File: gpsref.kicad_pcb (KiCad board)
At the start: 4 copper layers, 79.8 x 47.2 mm, 150 parts, among them J13 Boot, J2 SMA, J3 SMA, J4 SMA, J5 U.Fl, J6 SMA, J7 USB_C_Receptacle_16P, J8 U.Fl, J9 U.Fl, Q1 AO3400A, Q2 AO3401A, T2 MABA-010247-2R1250, U1 MAX-M10S, U11 74LVC1G07, U2 LMK05318BRGZR, U21 TMP117xxDRV, U3 TG5032CGN, U31 TLV3601DCKR, U32 TLV3601DCKR, U4 STM32H503KBUx, U5 TPS82084SIL, U6 TPS82084SIL, U7 TPS7A8801RTJR

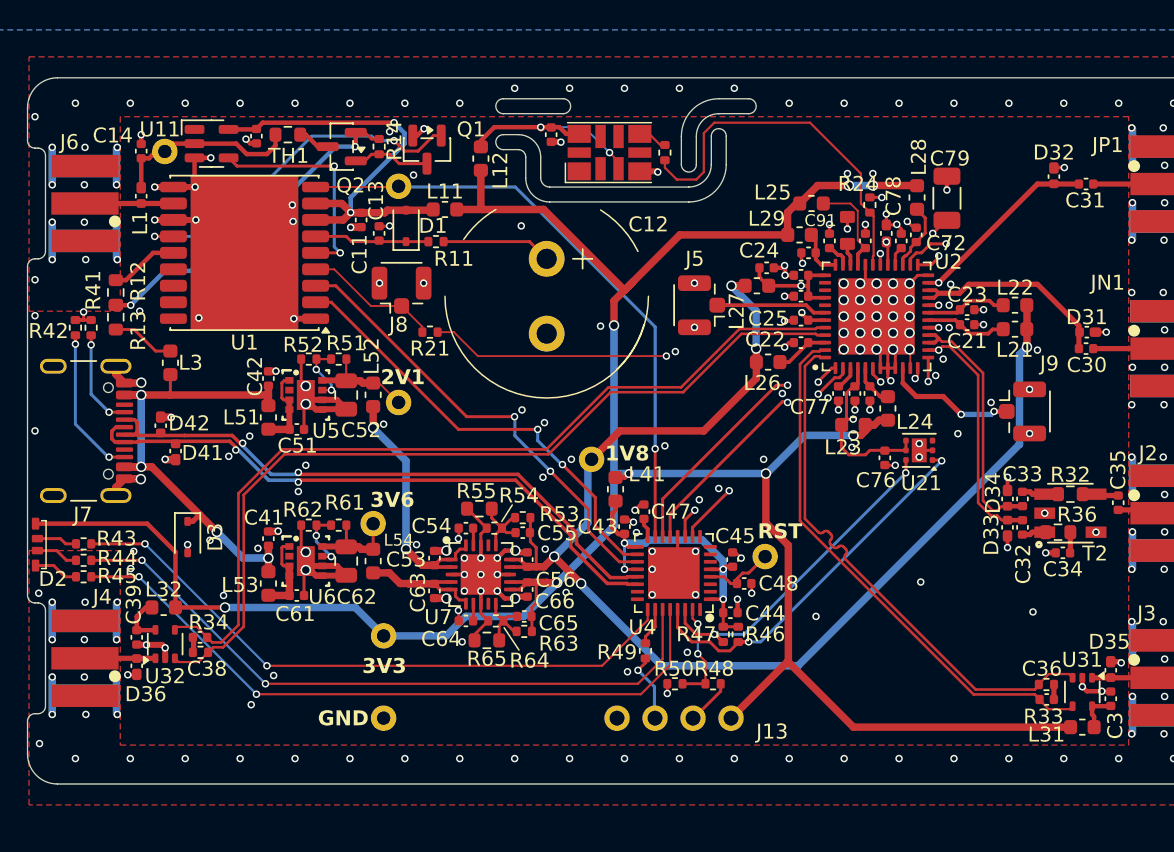
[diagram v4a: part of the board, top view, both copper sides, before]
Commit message: Skedd connector is back.
Route I2C to GPS and hook in the alert line.
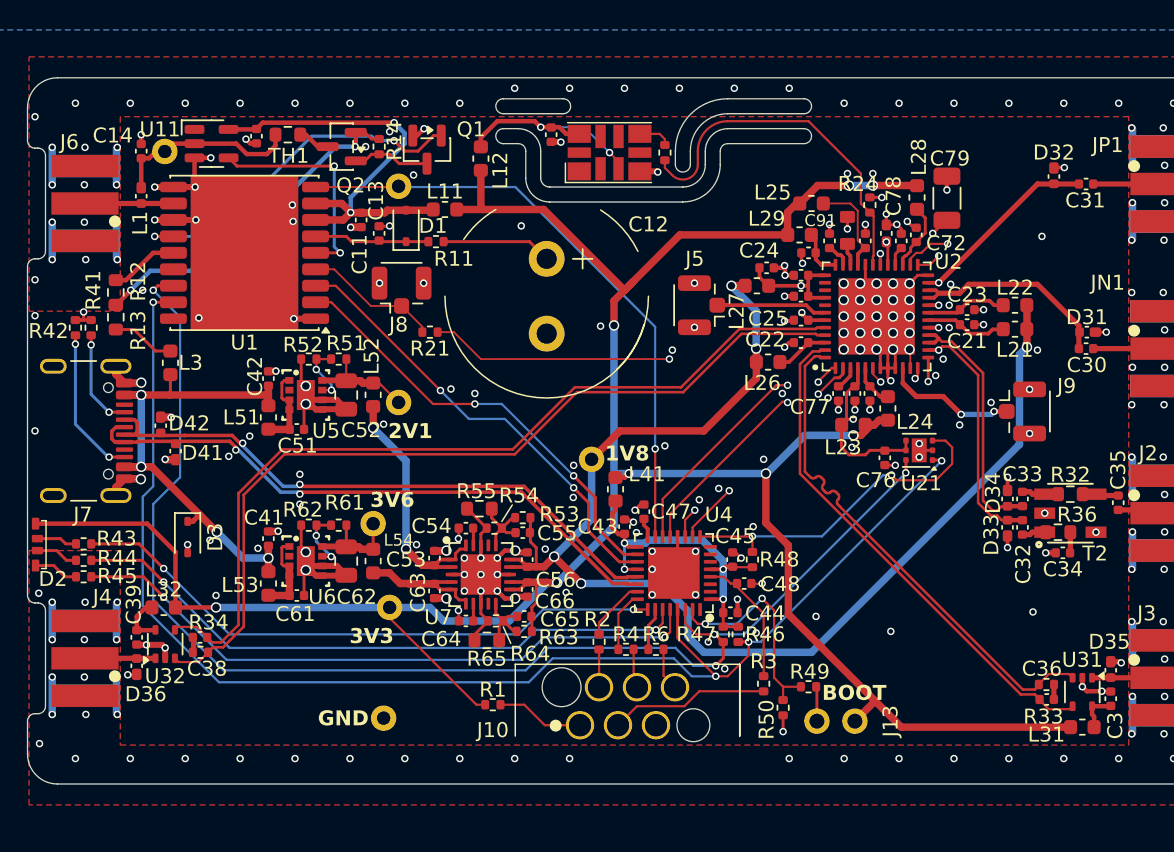
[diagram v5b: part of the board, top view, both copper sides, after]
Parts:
- removed the R49 at (140.1, 114.7)
- removed TP8: TestPoint_Probe, Parts:TestPoint
- added J10: Skedd, Parts:Skedd6, F.Cu at (138.9, 118.4)
- added R1: 100, Resistor_SMD:R_0402_1005Metric, F.Cu at (129.9, 118.3)
- added R2: 100, Resistor_SMD:R_0402_1005Metric, F.Cu at (137.0, 114.1)
- added R3: 100, Resistor_SMD:R_0402_1005Metric, F.Cu at (148.0, 116.9)
- added R4: 100, Resistor_SMD:R_0402_1005Metric, F.Cu at (138.8, 114.6)
- added R48: 10k, Resistor_SMD:R_0402_1005Metric, F.Cu at (147.2, 108.6)
- added R6: 100, Resistor_SMD:R_0402_1005Metric, F.Cu at (140.8, 114.6)
- J13: footprint Parts:PinHeader_1x04_P2.54mm_Vertical -> Parts:PinHeader_1x02_P2.54mm_Vertical
- moved J13 8.28 mm to (154.1, 119.4)
- moved R50 7.40 mm to (149.3, 118.5), turned to -90 degrees
- moved R49 6.38 mm to (151.0, 117.1)
- moved TP7 1.94 mm to (123.0, 111.8)
- renumbered R48 to R49
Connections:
- U1 pad 16: unconnected-(U1-SDA-Pad16) -> I2C_SDA
- U1 pad 17: unconnected-(U1-SCL-Pad17) -> I2C_SCL
- U21 pad 3: unconnected-(U21-ALERT-Pad3) -> ALERT
- U4 pad 23: unconnected-(U4-PA13(JTMS-Pad23) -> /CPU/SWDIO
- U4 pad 24: unconnected-(U4-PA14(JTCK-Pad24) -> /CPU/SWCLK
- U4 pad 9: unconnected-(U4-PA3-Pad9) -> ALERT
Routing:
- net I2C_SDA: track 43.1 -> 108.4 mm, vias 3 -> 5
- net I2C_SCL: track 47.4 -> 112.3 mm, vias 3 -> 5
- net ALERT: track 0.00 -> 22.8 mm, vias 0 -> 2
- net /CPU/dRST: track 0.00 -> 10.7 mm
- net /CPU/BOOT0: track 6.85 -> 14.7 mm
- net /Clocking/XO_P: track 24.9 -> 18.9 mm
- net /CPU/d3V3: track 0.00 -> 5.88 mm
- net /CPU/SWDIO: track 0.00 -> 4.20 mm
- net /CPU/CPU_nRST: track 4.78 -> 8.90 mm
- net /CPU/SWCLK: track 0.00 -> 4.06 mm
- net /CPU/Green: track 45.6 -> 42.2 mm
- net +3V3: track 171.4 -> 174.7 mm
- net /CPU/Red: track 46.5 -> 43.3 mm
- net /CPU/dSWC: track 0.00 -> 2.62 mm
- net /CPU/dSWD: track 0.00 -> 2.52 mm
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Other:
- outline, holes or cut-outs redrawn
- board text added: "BOOT"
- board text removed: "RST"

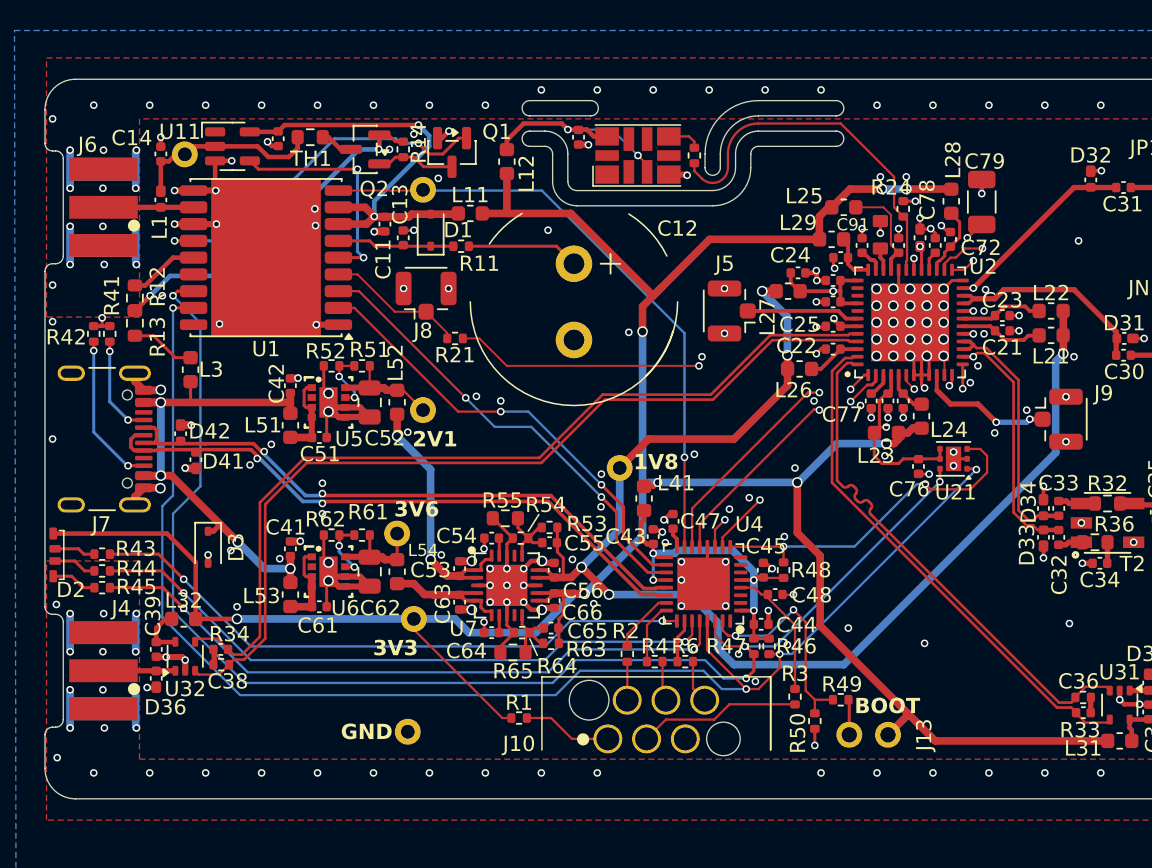
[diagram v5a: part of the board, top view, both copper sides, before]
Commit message: Route extint.
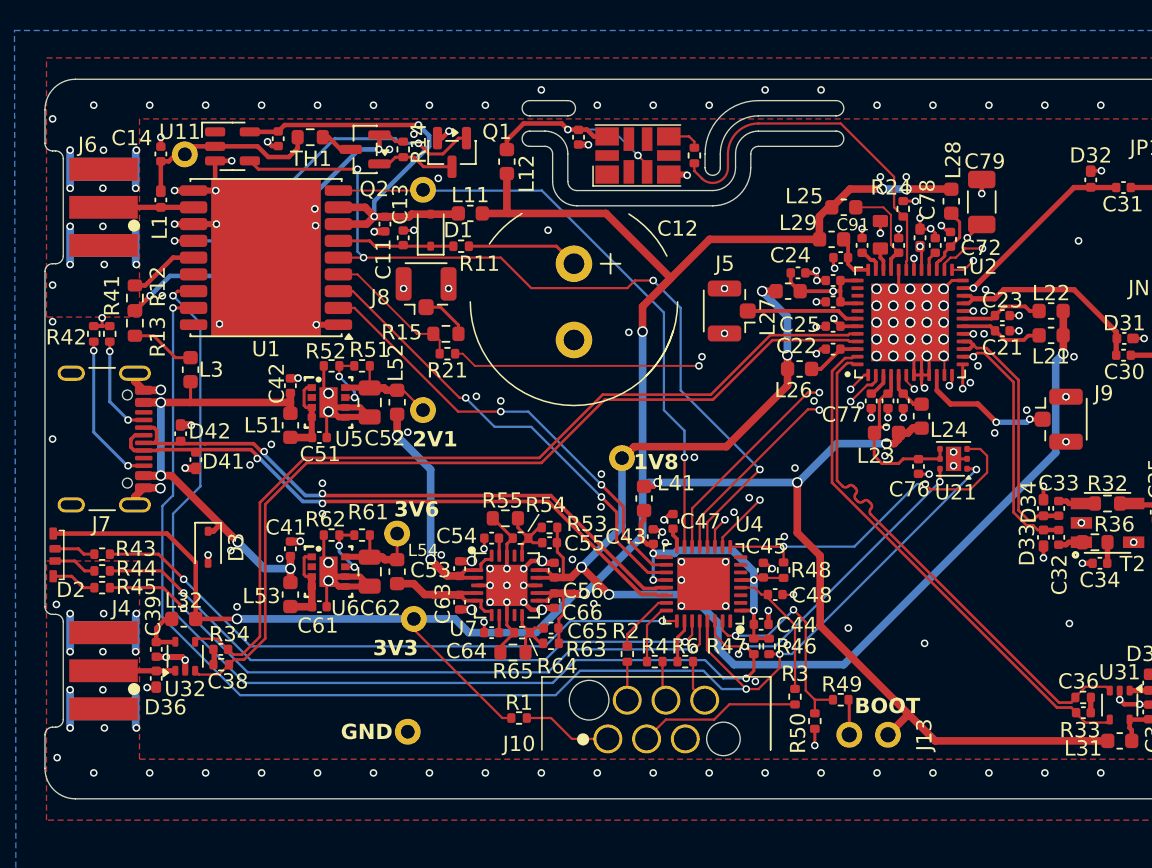
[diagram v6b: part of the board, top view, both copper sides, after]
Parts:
- added R15: 0, Resistor_SMD:R_0603_1608Metric, F.Cu at (125.1, 93.1)
- moved R21 1.12 mm to (125.2, 94.4)
- moved TP6 0.67 mm to (136.7, 101.2)
- moved J8 0.30 mm to (123.8, 90.3)
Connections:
- J8 pad 1: GPSCLK -> Net-(J8-In)
- U1 pad 5: /GPS/EXTINT -> EXTINT
- U11 pad 4: /GPS/EXTINT -> EXTINT
- U4 pad 12: GND -> EXTINT
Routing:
- net EXTINT: track 0.00 -> 56.7 mm, vias 0 -> 4
- net /GPS/EXTINT: track 14.9 -> 0.00 mm, vias 2 -> 0
- net Net-(J8-In): track 0.00 -> 3.19 mm
- net GND: track 168.7 -> 166.4 mm, vias 286 -> 289
- net OUT5: track 7.41 -> 8.04 mm
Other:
- outline, holes or cut-outs redrawn

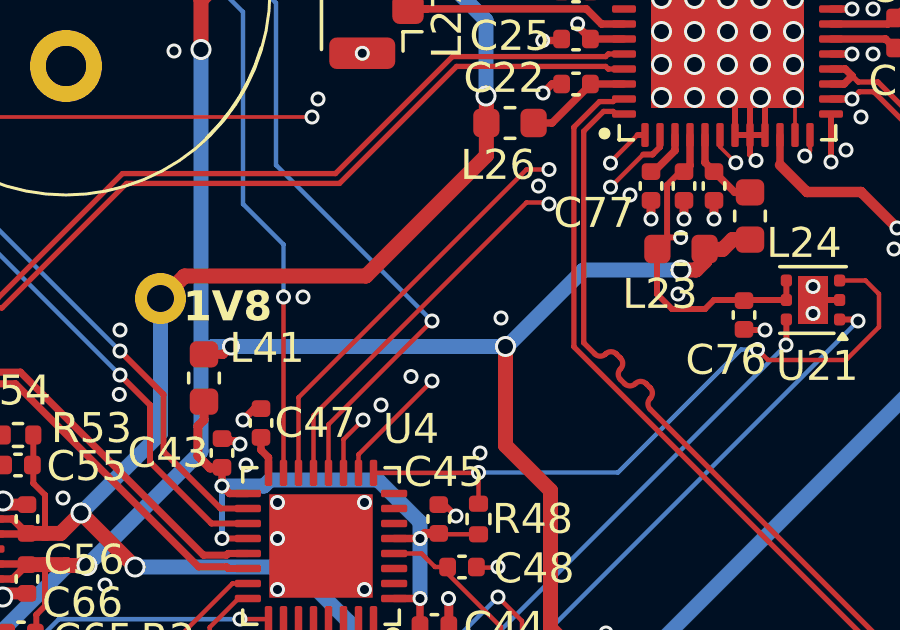
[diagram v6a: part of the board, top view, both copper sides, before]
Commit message: Nix a DRC error.
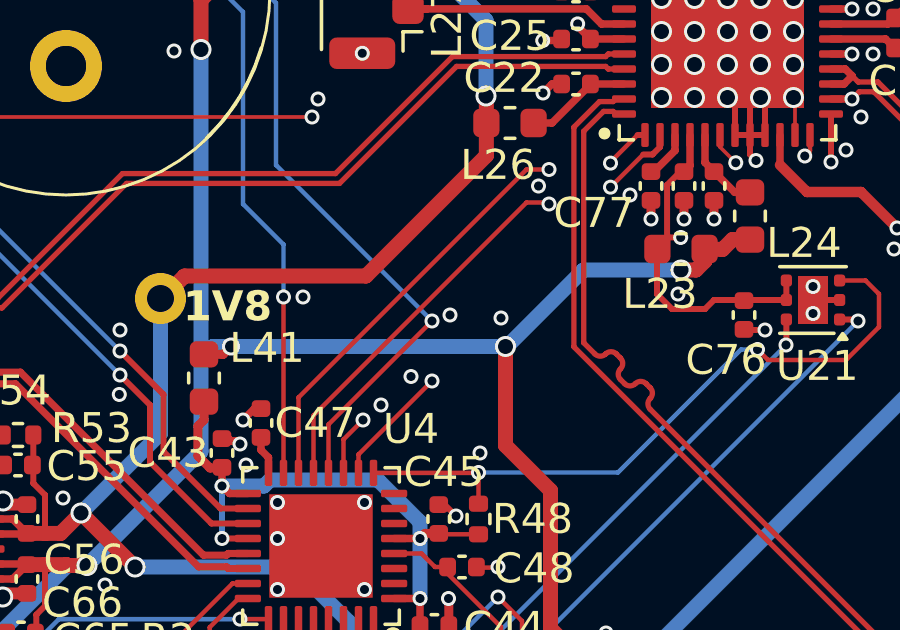
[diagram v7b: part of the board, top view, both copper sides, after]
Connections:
- C30 pad 1: OUT1_P -> OUT1_N
- C31 pad 1: OUT1_N -> OUT1_P
- D31 pad 1: OUT1_P -> OUT1_N
- D32 pad 1: OUT1_N -> OUT1_P
- U2 pad 20: OUT1_N -> OUT1_P
- U2 pad 21: OUT1_P -> OUT1_N
- U2 pad 22: OUT1_P -> OUT1_N
- U2 pad 23: OUT1_N -> OUT1_P
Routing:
- net OUT1_P: track 13.9 -> 15.0 mm, vias 0 -> 2
- net OUT1_N: track 15.0 -> 13.9 mm, vias 2 -> 0
- net GND: vias 289 -> 290
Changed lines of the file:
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@@
 			(layers "F.Cu" "F.Mask" "F.Paste")
 			(roundrect_rratio 0.25)
-			(net 91 "OUT1_N")
+			(net 90 "OUT1_P")
 			(pinfunction "A1")
 			(pintype "passive")
@@
 			(layers "F.Cu" "F.Mask" "F.Paste")
 			(roundrect_rratio 0.25)
-			(net 90 "OUT1_P")
+			(net 91 "OUT1_N")
 			(pintype "passive")
 		)
@@
 			(roundrect_rratio 0.25)
 			(net 66 "FDEC")
-			(pinfunction "STATUS1")
+			(pinfunction "_FDEC")
 			(pintype "bidirectional")
 		)
@@
 			(layers "F.Cu" "F.Mask" "F.Paste")
 			(roundrect_rratio 0.25)
-			(net 91 "OUT1_N")
+			(net 90 "OUT1_P")
 			(pinfunction "OUT2_P")
 			(pintype "output")
@@
 			(layers "F.Cu" "F.Mask" "F.Paste")
 			(roundrect_rratio 0.25)
-			(net 90 "OUT1_P")
+			(net 91 "OUT1_N")
 			(pinfunction "OUT2_N")
 			(pintype "output")
@@
 			(layers "F.Cu" "F.Mask" "F.Paste")
 			(roundrect_rratio 0.25)
-			(net 90 "OUT1_P")
+			(net 91 "OUT1_N")
 			(pinfunction "OUT3_N")
 			(pintype "output")
@@
 			(layers "F.Cu" "F.Mask" "F.Paste")
 			(roundrect_rratio 0.25)
-			(net 91 "OUT1_N")
+			(net 90 "OUT1_P")
 			(pinfunction "OUT3_P")
 			(pintype "output")
@@
 			(roundrect_rratio 0.25)
 			(net 64 "FINC")
-			(pinfunction "GPIO2")
+			(pinfunction "_FINC")
 			(pintype "bidirectional")
 		)
@@
 			(layers "F.Cu" "F.Mask" "F.Paste")
 			(roundrect_rratio 0.25)
-			(net 90 "OUT1_P")
+			(net 91 "OUT1_N")
 			(pinfunction "A1")
 			(pintype "passive")
@@
 			(layers "F.Cu" "F.Mask" "F.Paste")
 			(roundrect_rratio 0.25)
-			(net 91 "OUT1_N")
+			(net 90 "OUT1_P")
 			(pintype "passive")
 		)
@@
 	)
 	(via
+		(at 146.3 101.8)
+		(size 0.5)
+		(drill 0.3)
+		(layers "F.Cu" "B.Cu")
+		(free yes)
+		(net 1)
+	)
+	(via
 		(at 165.775 97.225)
 		(size 0.5)
@@
 	)
 	(segment
-		(start 161.1 90.8)
-		(end 161.7 90.2)
+		(start 159.7 90.1)
+		(end 166.3 83.5)
 		(width 0.3493)
 		(layer "F.Cu")
@@
 	)
 	(segment
-		(start 159.4 91.1)
-		(end 159.7 90.8)
+		(start 159 90.1)
+		(end 159.7 90.1)
 		(width 0.25)
 		(layer "F.Cu")
@@
 	)
 	(segment
-		(start 159.7 90.8)
-		(end 161.1 90.8)
-		(width 0.3493)
-		(layer "F.Cu")
-		(net 90)
-	)
-	(segment
-		(start 159.5 90.6)
-		(end 159.7 90.8)
+		(start 159 91.6)
+		(end 159.7 91.6)
 		(width 0.25)
 		(layer "F.Cu")
@@
 	)
 	(segment
-		(start 166.3 90.2)
-		(end 169.07 92.97)
+		(start 166.3 83.5)
+		(end 169.07 83.5)
 		(width 0.3493)
 		(layer "F.Cu")
 		(net 90)
 	)
-	(segment
-		(start 161.7 90.2)
-		(end 166.3 90.2)
-		(width 0.3493)
-		(layer "F.Cu")
+	(via
+		(at 159.7 91.6)
+		(size 0.5)
+		(drill 0.3)
+		(layers "F.Cu" "B.Cu")
 		(net 90)
 	)
-	(segment
-		(start 159 90.6)
-		(end 159.5 90.6)
-		(width 0.25)
-		(layer "F.Cu")
+	(via
+		(at 159.7 90.1)
+		(size 0.5)
+		(drill 0.3)
+		(layers "F.Cu" "B.Cu")
 		(net 90)
 	)
 	(segment
-		(start 159 91.1)
-		(end 159.4 91.1)
-		(width 0.25)
-		(layer "F.Cu")
+		(start 159.7 91.6)
+		(end 159.7 90.1)
+		(width 0.2761)
+		(layer "In2.Cu")
 		(net 90)
 	)
 	(segment
-		(start 169.07 92.97)
-		(end 169.07 94.5)
+		(start 161.1 90.8)
+		(end 161.7 90.2)
 		(width 0.3493)
 		(layer "F.Cu")
-		(net 90)
+		(net 91)
 	)
 	(segment
-		(start 159.7 90.1)
-		(end 166.3 83.5)
+		(start 159.4 91.1)
+		(end 159.7 90.8)
+		(width 0.25)
+		(layer "F.Cu")
+		(net 91)
+	)
+	(segment
+		(start 159.7 90.8)
+		(end 161.1 90.8)
 		(width 0.3493)
 		(layer "F.Cu")
@@
 	)
 	(segment
-		(start 159 90.1)
-		(end 159.7 90.1)
+		(start 159.5 90.6)
+		(end 159.7 90.8)
 		(width 0.25)
 		(layer "F.Cu")
@@
 	)
 	(segment
-		(start 159 91.6)
-		(end 159.7 91.6)
-		(width 0.25)
+		(start 166.3 90.2)
+		(end 169.07 92.97)
+		(width 0.3493)
 		(layer "F.Cu")
 		(net 91)
 	)
 	(segment
-		(start 166.3 83.5)
-		(end 169.07 83.5)
+		(start 161.7 90.2)
+		(end 166.3 90.2)
 		(width 0.3493)
 		(layer "F.Cu")
 		(net 91)
 	)
-	(via
-		(at 159.7 91.6)
-		(size 0.5)
-		(drill 0.3)
-		(layers "F.Cu" "B.Cu")
+	(segment
+		(start 159 90.6)
+		(end 159.5 90.6)
+		(width 0.25)
+		(layer "F.Cu")
 		(net 91)
 	)
-	(via
-		(at 159.7 90.1)
-		(size 0.5)
-		(drill 0.3)
-		(layers "F.Cu" "B.Cu")
+	(segment
+		(start 159 91.1)
+		(end 159.4 91.1)
+		(width 0.25)
+		(layer "F.Cu")
 		(net 91)
 	)
 	(segment
-		(start 159.7 91.6)
-		(end 159.7 90.1)
-		(width 0.2761)
-		(layer "In2.Cu")
+		(start 169.07 92.97)
+		(end 169.07 94.5)
+		(width 0.3493)
+		(layer "F.Cu")
 		(net 91)
 	)
@@
 		(polygon
 			(pts
-				(xy 124.75 89.035) (xy 124.75 91.1) (xy 122.852637 91.1) (xy 122.85 89.035)
+				(xy 124.750461 88.76) (xy 124.750461 90.825) (xy 122.853098 90.825) (xy 122.850461 88.76)
 			)
 		)
